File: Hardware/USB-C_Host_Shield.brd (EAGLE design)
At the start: 53.3 x 59.7 mm, 139 parts, among them J1 USB-C, J2 GPIN, J3 GPOUT, U1 ARDUINO_UNO_R3_SHIELDNOLABELS, U2 LM1117, U3 74HC4050, U5 MAX3421, U6 3.3V/150mA, Y1 12.0mhZ

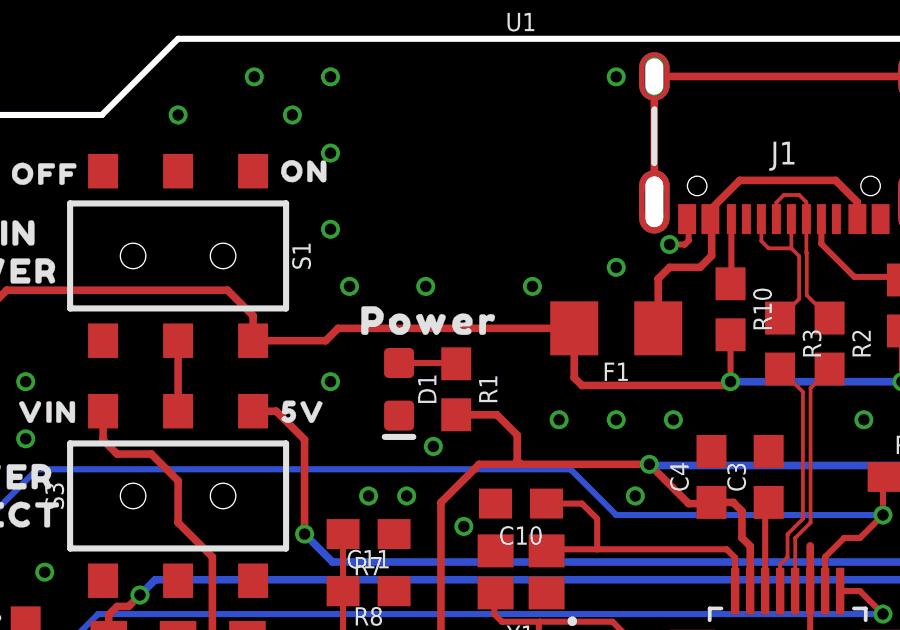
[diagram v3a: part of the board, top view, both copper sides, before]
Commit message: Updated layout with correct cap value
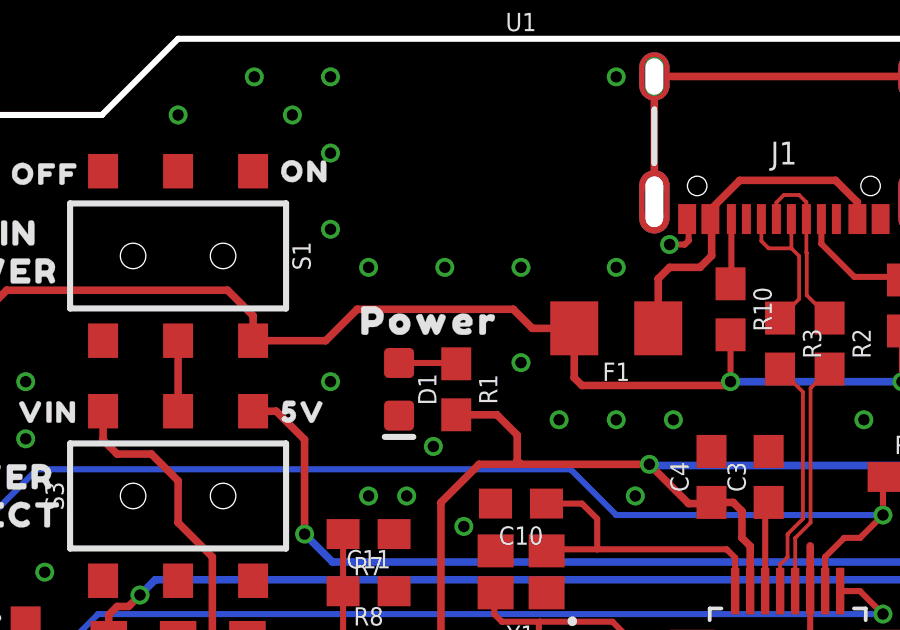
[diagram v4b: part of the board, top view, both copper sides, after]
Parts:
- C11: value 2.2uF -> 10uF
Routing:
- net VDD: track 50.3 -> 50.8 mm
- net GND: vias 105 -> 106
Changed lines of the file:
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@@
 <attribute name="VALUE" x="26.67" y="42.418" size="0.6096" layer="27" font="vector" ratio="20" rot="R180" align="top-center"/>
-</element>
-<element name="C11" library="SparkFun-Capacitors" package="0603" value="2.2uF" x="21.59" y="38.735" smashed="yes">
-<attribute name="NAME" x="21.59" y="39.497" size="0.6096" layer="25" font="vector" ratio="20" align="bottom-center"/>
-<attribute name="PROD_ID" value="CAP-07888" x="95.25" y="-59.055" size="1.778" layer="27" display="off"/>
-<attribute name="VALUE" x="21.59" y="37.973" size="0.6096" layer="27" font="vector" ratio="20" align="top-center"/>
 </element>
 <element name="C6" library="SparkFun-Capacitors" package="EIA3216" value="10uF" x="8.89" y="33.02" smashed="yes">
@@
 <attribute name="PROD_ID" value="RES-11150" x="29.845" y="47.498" size="1.778" layer="27" font="vector" ratio="15" rot="R180" display="off"/>
 <attribute name="VALUE" x="29.845" y="48.641" size="0.6096" layer="27" font="vector" ratio="20" rot="R180" align="top-center"/>
+</element>
+<element name="C11" library="SparkFun-Capacitors" package="0603" value="10uF" x="21.59" y="38.735" smashed="yes">
+<attribute name="NAME" x="21.59" y="39.497" size="0.6096" layer="25" font="vector" ratio="20" align="bottom-center"/>
+<attribute name="PROD_ID" value="CAP-11015" x="21.59" y="38.735" size="1.778" layer="27" font="vector" ratio="15" display="off"/>
+<attribute name="VALUE" x="21.59" y="37.973" size="0.6096" layer="27" font="vector" ratio="20" align="top-center"/>
 </element>
 </elements>
@@
 <via x="12.065" y="29.845" extent="1-16" drill="0.381"/>
 <via x="5.08" y="29.21" extent="1-16" drill="0.381"/>
-<via x="23.495" y="48.895" extent="1-16" drill="0.381"/>
-<via x="27.051" y="48.895" extent="1-16" drill="0.381"/>
+<via x="24.13" y="49.53" extent="1-16" drill="0.381"/>
+<via x="26.67" y="49.53" extent="1-16" drill="0.381"/>
 <via x="27.94" y="44.45" extent="1-16" drill="0.381"/>
 <via x="31.75" y="44.45" extent="1-16" drill="0.381"/>
@@
 <via x="5.08" y="45.72" extent="1-16" drill="0.381"/>
 <via x="10.16" y="45.72" extent="1-16" drill="0.381"/>
-<via x="20.955" y="48.895" extent="1-16" drill="0.381"/>
+<via x="21.59" y="49.53" extent="1-16" drill="0.381"/>
 <via x="20.32" y="45.72" extent="1-16" drill="0.381"/>
 <via x="23.749" y="43.561" extent="1-16" drill="0.381"/>
@@
 <contactref element="C5" pad="2"/>
 <contactref element="C4" pad="2"/>
-<contactref element="C11" pad="2"/>
 <contactref element="R7" pad="1"/>
 <contactref element="U5" pad="19"/>
@@
 <via x="38.1" y="44.45" extent="1-16" drill="0.381"/>
 <via x="20.32" y="50.8" extent="1-16" drill="0.381"/>
+<via x="26.67" y="46.355" extent="1-16" drill="0.381"/>
+<contactref element="C11" pad="2"/>
 </signal>
 <signal name="N$7">
@@
 <contactref element="R7" pad="2"/>
 <contactref element="R8" pad="1"/>
+<wire x1="18.3388" y1="36.6268" x2="17.5514" y2="36.6268" width="0.2032" layer="1"/>
+<wire x1="20.74" y1="36.83" x2="18.542" y2="36.83" width="0.2032" layer="1"/>
+<wire x1="18.542" y1="36.83" x2="18.3388" y2="36.6268" width="0.2032" layer="1"/>
 <contactref element="C11" pad="1"/>
 <wire x1="20.74" y1="36.83" x2="20.74" y2="38.735" width="0.2032" layer="1"/>
 <wire x1="20.74" y1="38.735" x2="20.74" y2="40.64" width="0.2032" layer="1"/>
-<wire x1="18.3388" y1="36.6268" x2="17.5514" y2="36.6268" width="0.2032" layer="1"/>
-<wire x1="20.74" y1="36.83" x2="18.542" y2="36.83" width="0.2032" layer="1"/>
-<wire x1="18.542" y1="36.83" x2="18.3388" y2="36.6268" width="0.2032" layer="1"/>
 </signal>
 <signal name="RESET">
@@
 <wire x1="9.525" y1="48.768" x2="16.891" y2="48.768" width="0.254" layer="1"/>
 <wire x1="16.891" y1="48.768" x2="17.74" y2="47.919" width="0.254" layer="1"/>
-<wire x1="20.162" y1="47.086" x2="20.574" y2="47.498" width="0.254" layer="1"/>
+<wire x1="20.162" y1="47.086" x2="21.209" y2="48.133" width="0.254" layer="1"/>
 <wire x1="17.74" y1="47.086" x2="20.162" y2="47.086" width="0.254" layer="1"/>
-<wire x1="28.445" y1="47.498" x2="20.574" y2="47.498" width="0.254" layer="1"/>
+<wire x1="28.445" y1="47.498" x2="27.048" y2="47.498" width="0.254" layer="1"/>
+<wire x1="27.048" y1="47.498" x2="26.413" y2="48.133" width="0.254" layer="1"/>
+<wire x1="26.413" y1="48.133" x2="21.209" y2="48.133" width="0.254" layer="1"/>
 <wire x1="28.445" y1="45.85" x2="28.702" y2="45.593" width="0.254" layer="1"/>
 <wire x1="28.702" y1="45.593" x2="33.528" y2="45.593" width="0.254" layer="1"/>

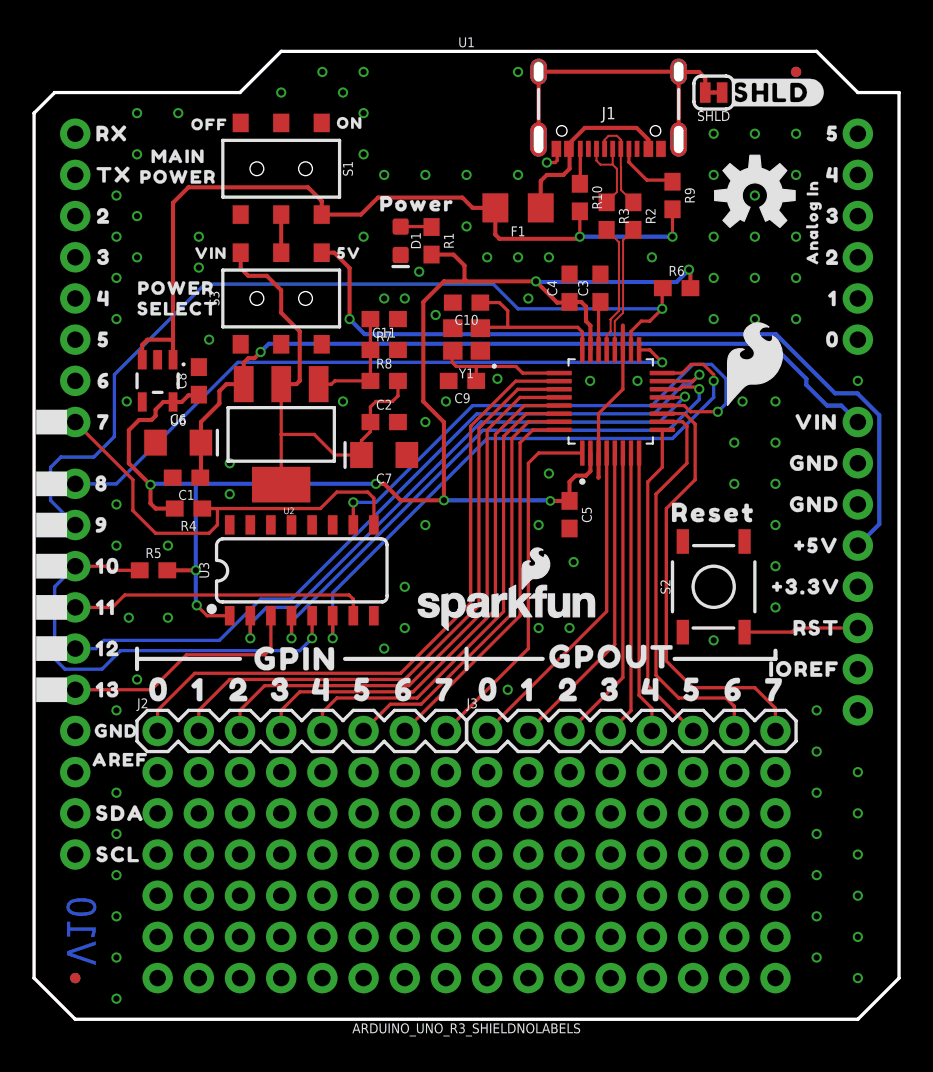
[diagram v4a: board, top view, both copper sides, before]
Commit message: Update board layout
Added thermal vias under LD1117, moved components away from LD1117, increased power trace width size
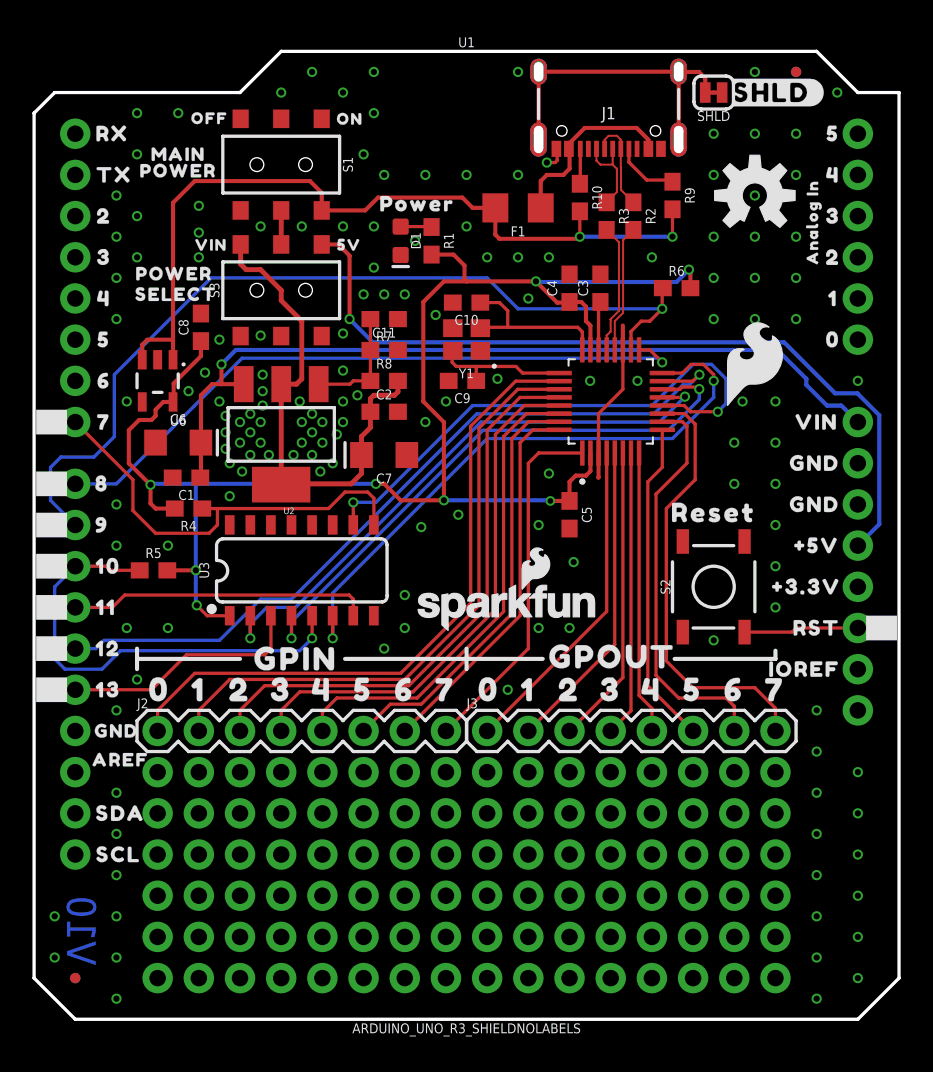
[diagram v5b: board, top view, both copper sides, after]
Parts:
- moved C8 3.30 mm to (10.3, 40.1)
- moved U$13 0.90 mm to (8.76, 42.2)
- moved U$10 0.90 mm to (8.64, 43.4)
- moved C2 0.63 mm to (21.6, 34.9)
- moved S3 0.51 mm to (15.2, 42.4)
- moved U$1 0.51 mm to (19.4, 45.2)
- moved U$12 0.51 mm to (10.9, 45.2)
- moved U$14 0.38 mm to (8.89, 49.8)
- moved U$7 0.38 mm to (10.8, 53.0)
- moved U$5 0.25 mm to (19.5, 53.0)
- moved S1 0.25 mm to (15.2, 50.2)
- moved U$15 0.13 mm to (8.89, 50.8)
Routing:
- net 3.3V: track 95.0 -> 97.7 mm
- net VIN: track 49.4 -> 50.9 mm
- net N$6: track 29.1 -> 30.6 mm
- net 5V: track 49.0 -> 49.6 mm
- net GND: vias 106 -> 153

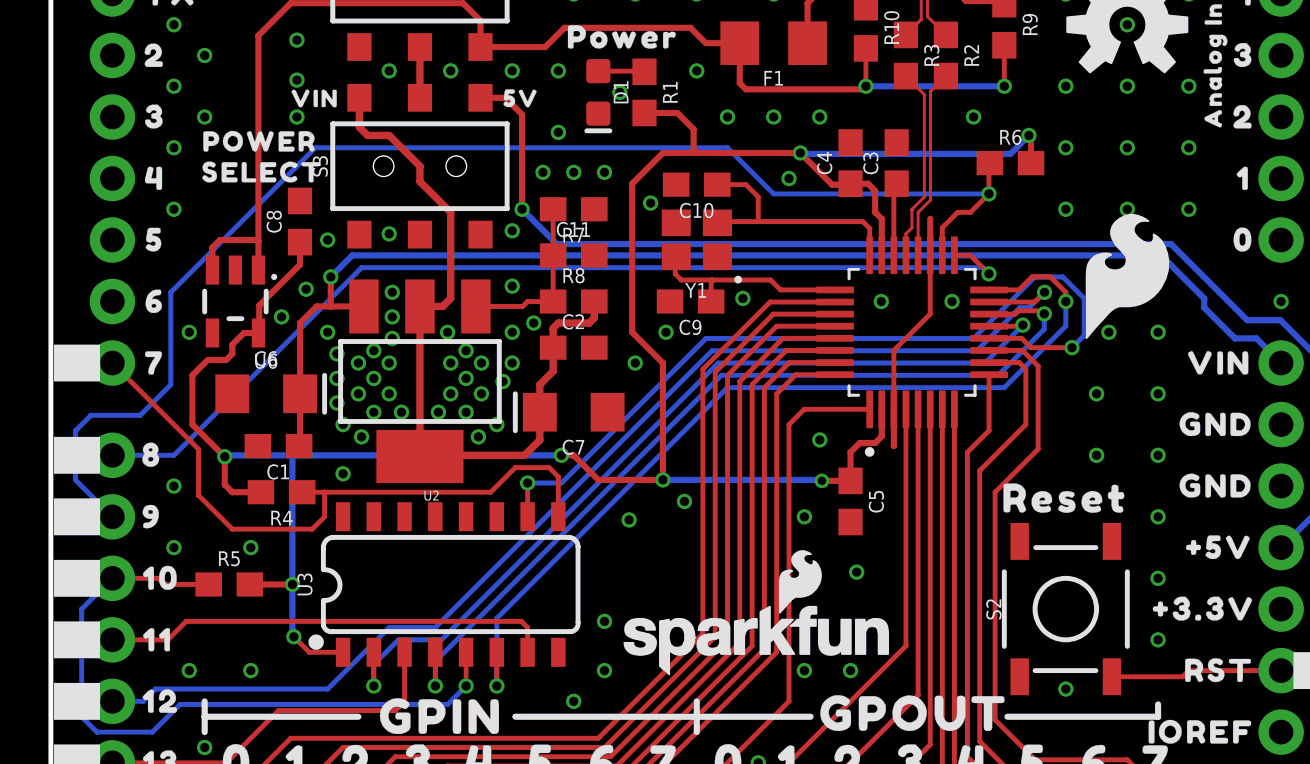
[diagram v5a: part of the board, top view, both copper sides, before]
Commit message: Update Board with thermal vias
Added more thermal vias under the LD1117 and adjusted traces accordingly
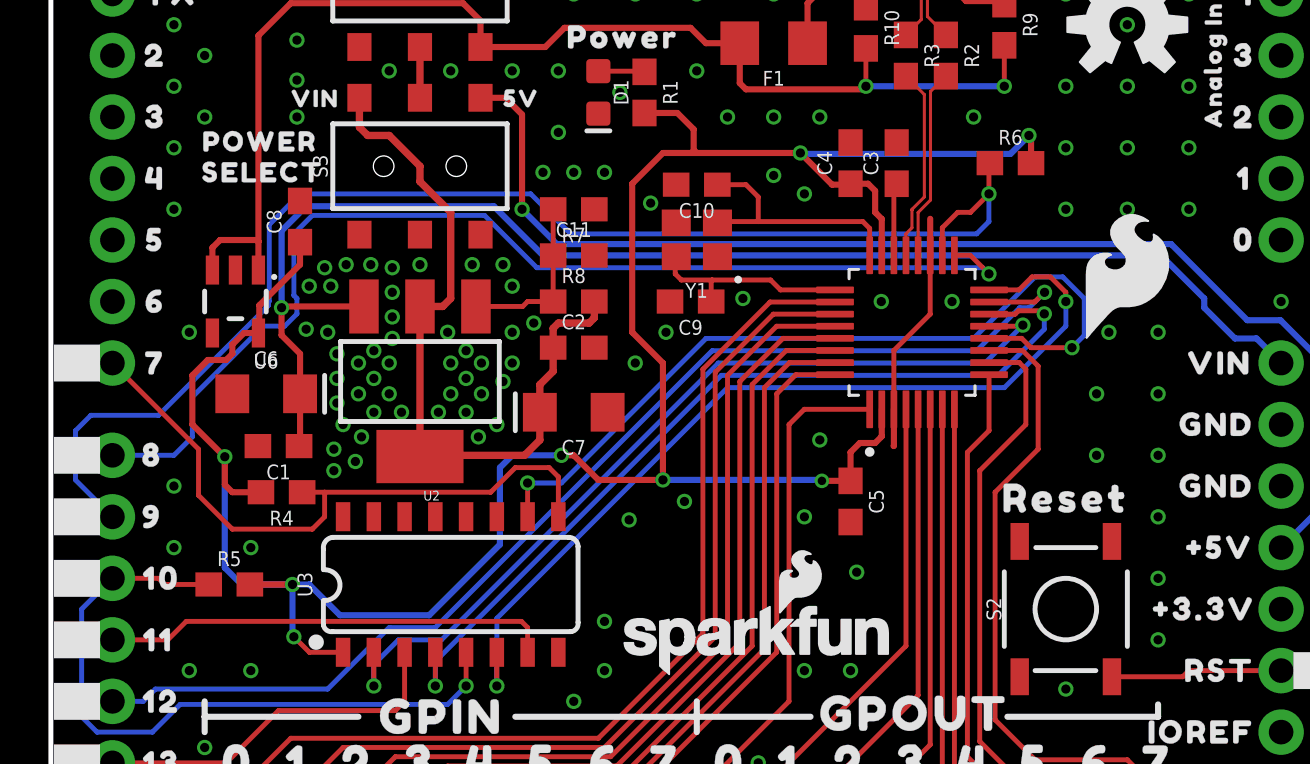
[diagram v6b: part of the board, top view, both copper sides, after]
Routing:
- net VIN: track 50.9 -> 57.3 mm
- net GPX: track 41.3 -> 46.1 mm
- net 3.3V: track 97.7 -> 102.3 mm
- net GND: vias 153 -> 161
